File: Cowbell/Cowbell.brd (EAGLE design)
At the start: 100 x 50 mm, 70 parts, among them IC1 LM741P, Q1 2N3906, T1 2N3904, T2 2N3904, T3 2N3904, T4 2N3904, T5 2N3904, T6 2N3904, T7 2N3904, T8 2N3904

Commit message: Placed parts on .brd file. Have to route yet.
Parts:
- removed 2.47K: 100, rcl:0207/7
- added R31: 2.47k, rcl:0207/7
- added U$1, U$2, U$3, U$4: (no value), ARVP:STAND-OFF
- added U$6: (no value), frames:A5L-LOC
- moved R2 166.9 mm to (16.0, 18.0)
- moved R26 114.4 mm to (64.0, 20.0), turned to 90 degrees
- moved SV1 111.8 mm to (25.0, 8.00), flipped to the bottom, turned to 180 degrees
- moved C1 107.4 mm to (9.00, 24.0), turned to 270 degrees
- moved R27 105.4 mm to (68.0, 20.0), turned to 90 degrees
- moved Q1 105.2 mm to (65.0, 28.0), turned to 270 degrees
- moved T8 101.5 mm to (70.0, 12.0), turned to 180 degrees
- moved R14 99.9 mm to (30.0, 31.0), turned to 180 degrees
- moved R28 99.3 mm to (72.0, 20.0), turned to 90 degrees
- moved R16 98.2 mm to (30.0, 35.0), turned to 180 degrees
- moved C2 95.9 mm to (23.0, 28.0), turned to 270 degrees
- moved R13 91.4 mm to (30.0, 27.0), turned to 180 degrees
- moved R30 91.1 mm to (78.0, 11.0)
- moved R29 90.8 mm to (76.0, 20.0), turned to 90 degrees
- moved C5 90.2 mm to (37.0, 41.0), turned to 270 degrees
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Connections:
- net -12V: now also R31.1; no longer 2.47K.1
- net N$31: now also R31.2; no longer 2.47K.2
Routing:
- added copper zone on layer 1, net GND
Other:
- board text added: "Andrew Schroeder"
- board text added: "REV 1.0"

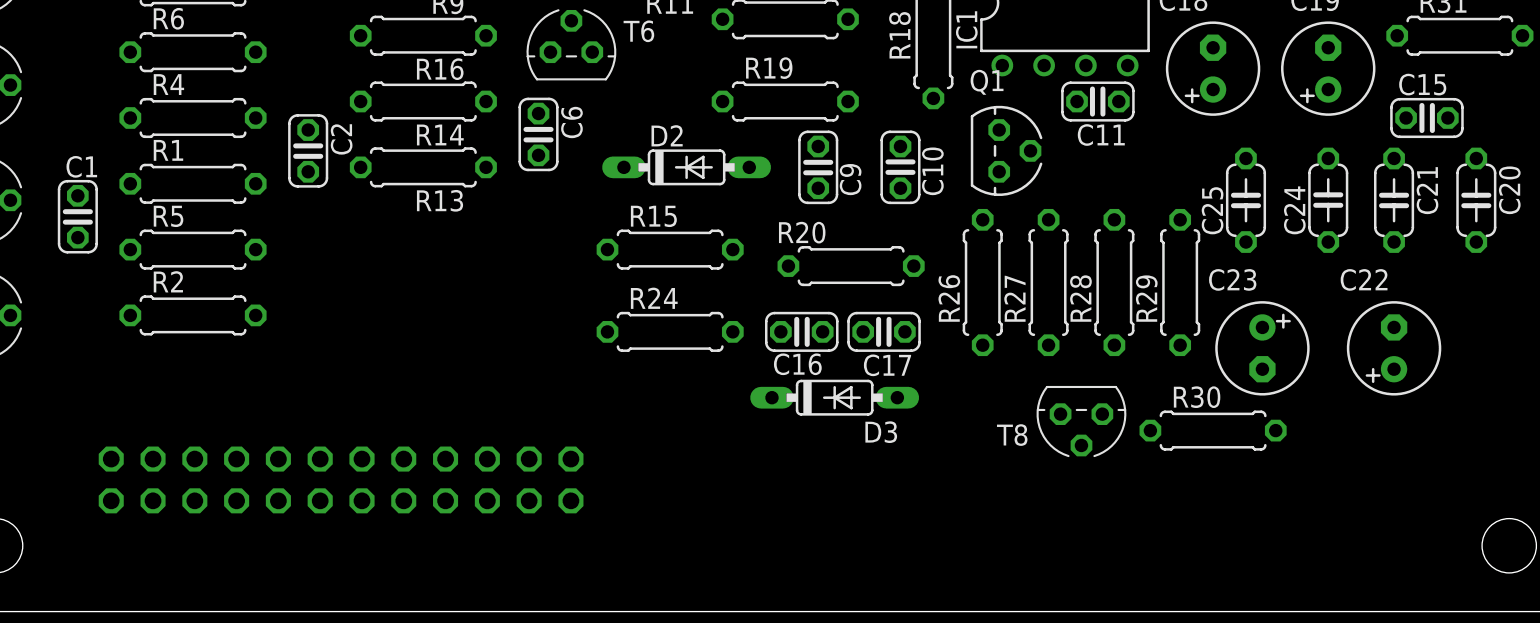
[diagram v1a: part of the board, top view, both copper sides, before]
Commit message: Repositioned main header.
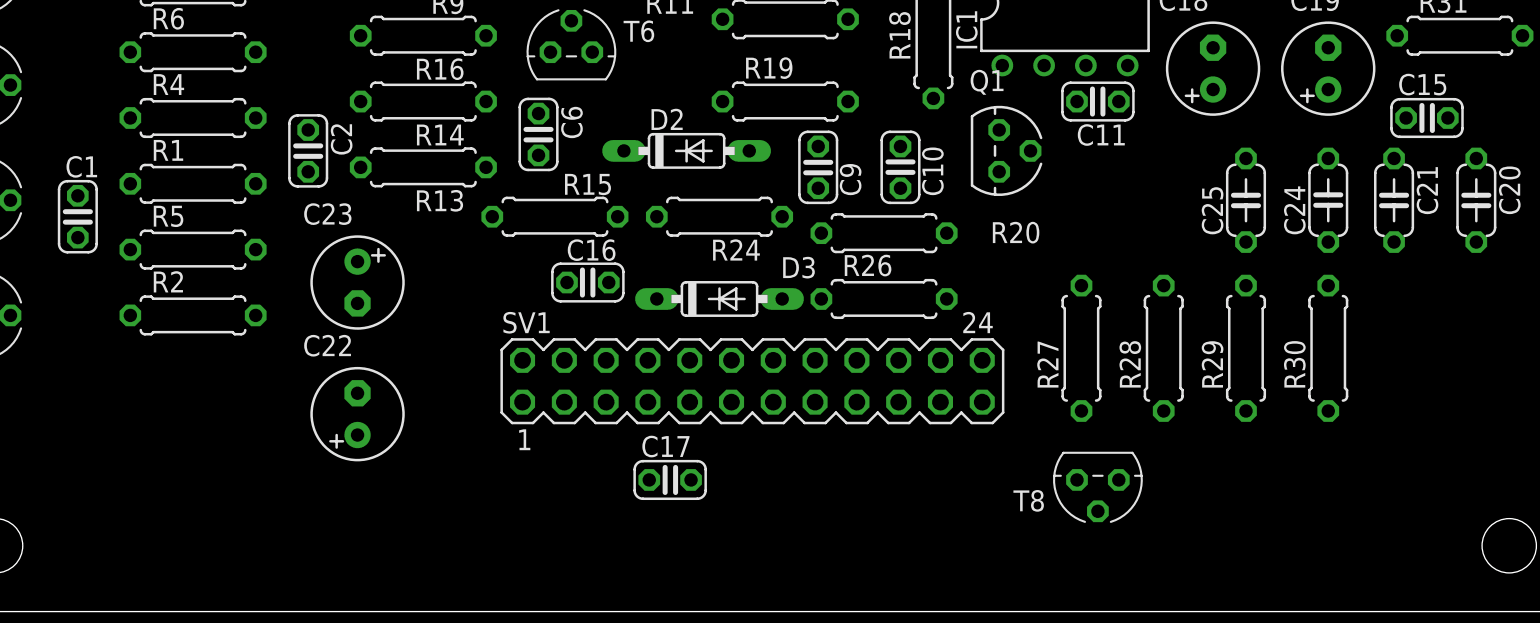
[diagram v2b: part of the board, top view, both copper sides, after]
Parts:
- moved C22 63.1 mm to (26.0, 12.0)
- moved C23 55.1 mm to (26.0, 20.0)
- moved SV1 25.7 mm to (50.0, 14.0), flipped to the top, turned to 0 degrees
- moved C17 15.8 mm to (45.0, 8.00), turned to 0 degrees
- moved C16 13.3 mm to (40.0, 20.0), turned to 180 degrees
- moved D3 9.22 mm to (48.0, 19.0)
- moved R30 8.60 mm to (85.0, 16.0), turned to 270 degrees
- moved R24 7.62 mm to (48.0, 24.0), turned to 180 degrees
- moved R15 7.28 mm to (38.0, 24.0), turned to 180 degrees
- moved R26 6.08 mm to (58.0, 19.0), turned to 0 degrees
- moved R29 5.66 mm to (80.0, 16.0)
- moved R28 5.00 mm to (75.0, 16.0)
- moved R27 4.47 mm to (70.0, 16.0)
- moved T8 4.12 mm to (71.0, 8.00)
- moved R20 2.83 mm to (58.0, 23.0)
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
